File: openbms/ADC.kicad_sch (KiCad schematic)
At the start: 117 parts, among them U1 DMP68D1LVQ-7, U10 DMP68D1LVQ-7, U11 DMN601VK-7, U12 DMN601VK-7, U13 DMN601VK-7, U14 DMN601VK-7, U2 DMP68D1LVQ-7, U3 DMN601VK-7, U4 DMP68D1LVQ-7, U5 ADS131M08xPBS, U6 DMP68D1LVQ-7, U7 DMN601VK-7, U8 DMP68D1LVQ-7, U9 DMP68D1LVQ-7, Y1 8.192MHz

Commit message: Footprints for pmos/nmos and pmos/pmos packages fixed, charger detection added, pwr_gd and flt_gd lines removed
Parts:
- U5: footprint custom_library:TQFP-32_5x5mm_P0.5mm -> Package_QFP:TQFP-32_5x5mm_P0.5mm
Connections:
- net CELL_6_M: now also U14.6; no longer U14.3
- net CELL_7_M: now also U14.3; no longer U14.6
- net GND: no longer R15.1, R16.1, R36.1, R37.1, R60.1, R61.1, R73.1, R77.1
- net GND_BATT_CELL: now also R15.1, R16.1, R36.1, R37.1, R60.1, R61.1, R73.1, R77.1
- net at R66.2, U10.5: now also U11.6; no longer U11.3
- net at U1.3: now also R11.2; no longer R10.2
- net at U1.6: now also R10.2; no longer R11.2
- net at R69.2: now also U10.3; no longer U10.6
- net at R28.2: now also U4.3; no longer U4.6
- net at D1.3 (K), D2.3 (K), D3.3 (K): now also U11.3; no longer U11.6
- net at U2.3: now also R13.2; no longer R12.2
- net at U2.6: now also R12.2; no longer R13.2
- net at U6.3: now also R42.2; no longer R41.2
- net at U6.6: now also R41.2; no longer R42.2
- net at R67.2: now also U9.6; no longer U9.3
- net at U8.3: now also R57.2; no longer R56.2
- net at U8.6: now also R56.2; no longer R57.2
- net at U3.3: now also R7.1; no longer R6.1
- net at U3.6: now also R6.1; no longer R7.1
- net at R68.2: now also U9.3; no longer U9.6
- net at R64.1: now also U12.6; no longer U12.3
- net at R34.1: now also U7.6; no longer U7.3
- net at R27.2: now also U4.6; no longer U4.3
- net at R74.1: now also U13.6; no longer U13.3
- net at R35.1: now also U7.3; no longer U7.6
- net at R65.1: now also U12.3; no longer U12.6

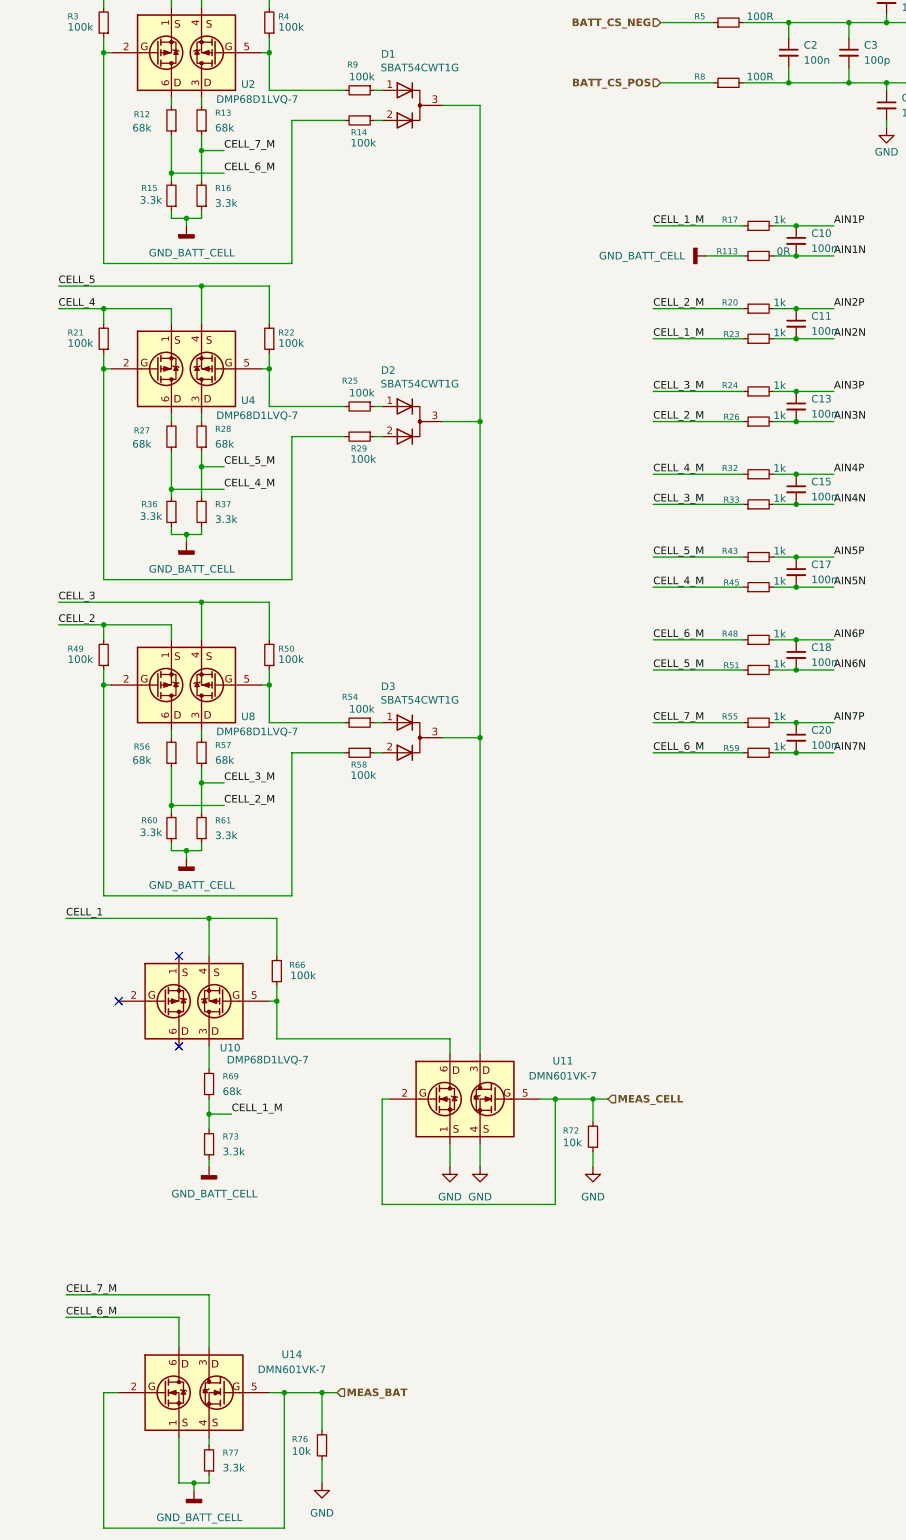
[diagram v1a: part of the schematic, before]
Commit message: Resistor dividers updated and put to 0.1% tolerance
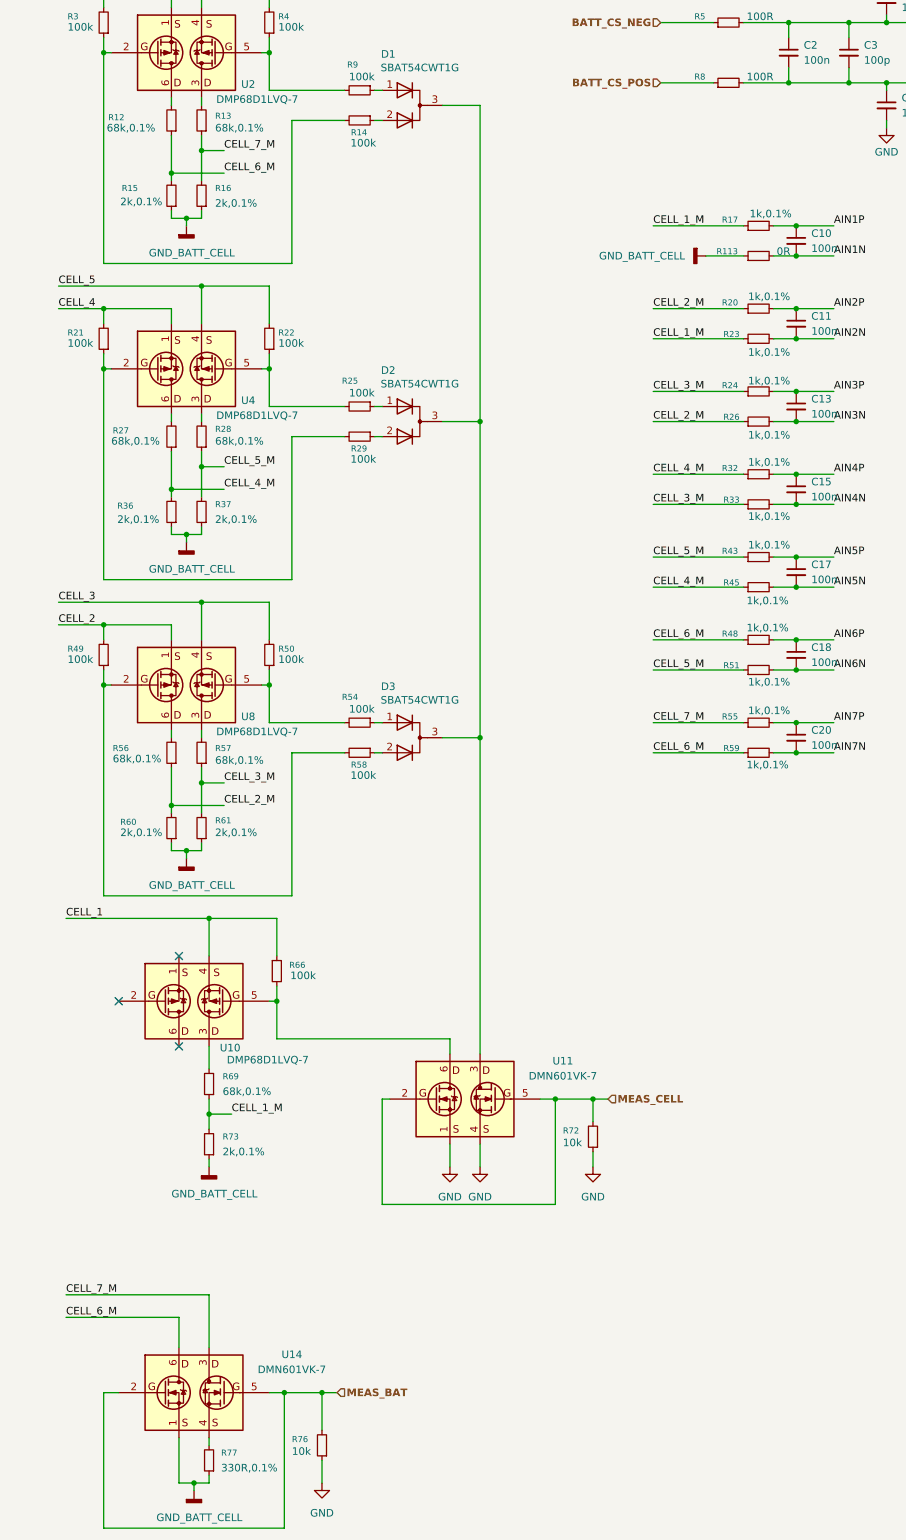
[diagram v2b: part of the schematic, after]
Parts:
- R12, R13, R27, R28, R56, R57, R69: value 68k -> 68k,0.1%; Manufacturer_Part_Number RMCF0402FT68K0 -> RT0402BRD0768KL
- R15, R16, R36, R37, R60, R61, R73: value 3.3k -> 2k,0.1%; Manufacturer_Part_Number ERA-2AEB332X -> RT0402BRD072KL
- R17, R20, R23, R24, R26, R32, R33, R43, R45, R48, R51, R55, R59: value 1k -> 1k,0.1%; Manufacturer_Part_Number RMCF0402FT1K00 -> RT0402BRD071KL
- R77: value 3.3k -> 330R,0.1%; Manufacturer_Part_Number ERA-2AEB332X -> RT0402BRD07330RL

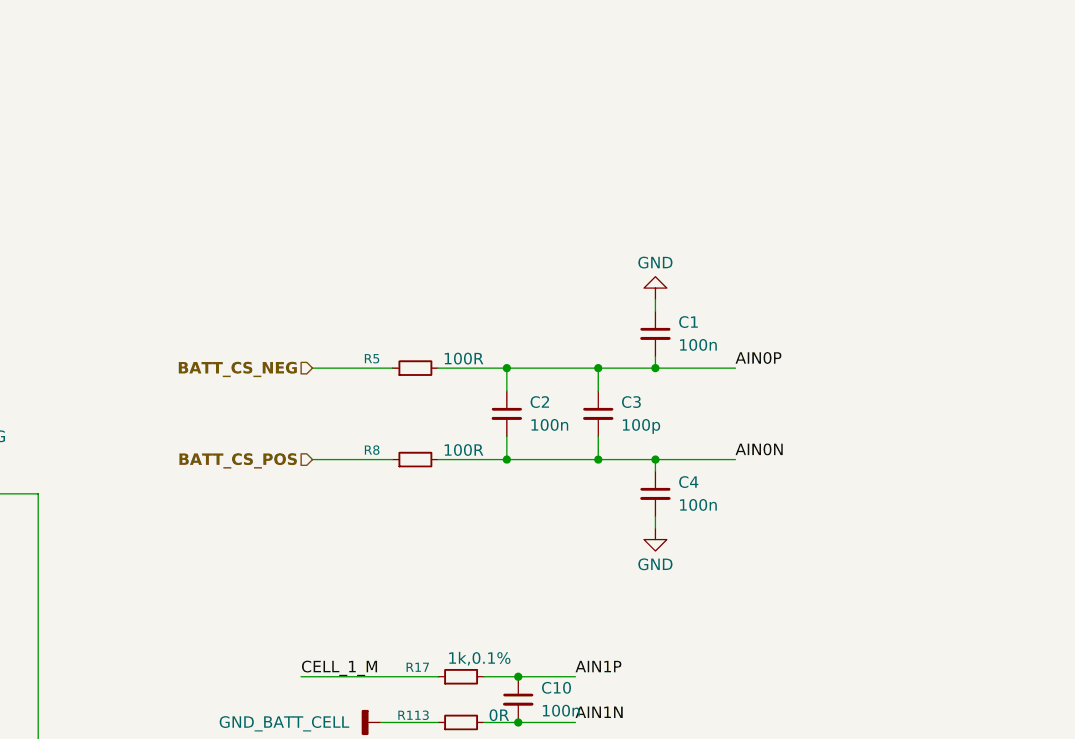
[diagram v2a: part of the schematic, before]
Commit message: Option to shortcut current ADC sensor added
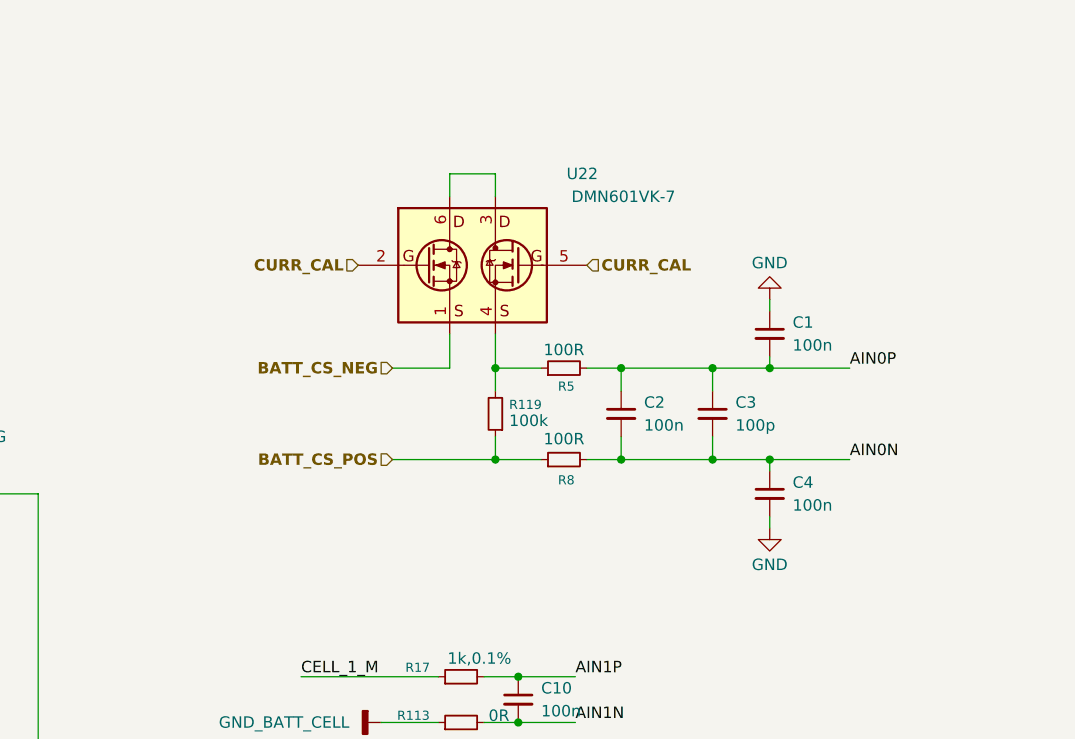
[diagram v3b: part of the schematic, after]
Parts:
- added R119: 100k, Resistor_SMD:R_0402_1005Metric, symbol Device:R_Small
- added U22: DMN601VK-7, custom_library:SOTFL50P162X60-6N, symbol custom_library:DMN601VK-7
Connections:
- net BATT_CS_NEG: now also U22.1; no longer R5.1
- net BATT_CS_POS: now also R119.1
- new net: R119.2, R5.1, U22.4
- new net: U22.3, U22.6
- new net CURR_CAL: U22.2, U22.5
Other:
- moved on the sheet: C1, C2, C3, C4, R5, R8

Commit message: Button for quick enable added
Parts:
- U5: footprint Package_QFP:TQFP-32_5x5mm_P0.5mm -> custom_library:TQFP-32_5x5mm_P0.5mm
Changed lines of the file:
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@@
 			)
 		)
-		(property "Footprint" "Package_QFP:TQFP-32_5x5mm_P0.5mm"
+		(property "Footprint" "custom_library:TQFP-32_5x5mm_P0.5mm"
 			(at 494.03 255.27 0)
 			(effects

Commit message: Green LED part number fixed,  PCB mask color updated, project description updated
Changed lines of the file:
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@@
 	(title_block
 		(title "OpenBMS")
-		(date "2026-03-24")
-		(rev "A")
+		(date "2026-09-24")
+		(rev "B")
 		(comment 2 "More at openbatt.dev")
 		(comment 3 "Designed by OpenBatt team")
@@
 		)
 	)
-	(text_box "About:\n- ADC circuit for battery voltage and current reading\n- Cell FETs for cell balancing\n\nDesign Parameters:\n- 7-cell battery voltage monitoring (between 2.5V and 4.3V)\n- 7-cell battery balancing (up to 86mA per cell)\n- Current monitoring (up to 20A)\n\nHow to use it:\n1) Battery cells are disabled from ADC by default to disable current leaking from battery when BMS is off. To enable battery reading, set MEAS_CELL to 1\n2) Read differential AINxP - AINxN voltage and multiply with 71.3/3.3 = 21.606 to get batter cell voltage in V\n3) Read battery current by reading voltage between AIN0P and AIN0N. Divide voltage by 0.001 (shunt resisot is 1m ohm) to get current in A\n4) There is a special case to read overall battery voltage by setting MEAS_BATT to 1 (while keeping MEAS_CELL at 1) and read voltage between AIN7P and AIN7N (like you would read cell 7) and multiply result with 74.6/6.6 = 11.303\n5) Balancing circuit for each sell can be enabled individually by setting CELL_x_BAL to 1. While balancer (cell FET) is on, don't read battery voltage, as you could get less precise cell voltage\n"
+	(text_box "About:\n- ADC circuit for battery voltage and current reading\n- Cell FETs for cell balancing\n\nDesign Parameters:\n- 7-cell battery voltage monitoring (between 2.5V and 4.3V)\n- 7-cell battery balancing (up to 86mA per cell)\n- Current monitoring (up to 20A)\n\nHow to use it:\n1) Battery cells are disabled from ADC by default to disable current leaking from battery when BMS is off. To enable battery reading, set MEAS_CELL to 1\n2) Read differential AINxP - AINxN voltage and multiply with (68+2)/2 = 35 to get batter cell voltage in V\n3) Read battery current by reading voltage between AIN0P and AIN0N. Divide voltage by 0.002 (shunt resisot is 2m ohm) to get current in A\n4) There is a special case to read overall battery voltage by setting MEAS_BATT to 1 (while keeping MEAS_CELL at 1) and read voltage between AIN7P and AIN7N (like you would read cell 7)\n5) Balancing circuit for each sell can be enabled individually by setting CELL_x_BAL to 1. While balancer (cell FET) is on, don't read battery voltage, as you could get less precise cell voltage\n"
 		(exclude_from_sim no)
 		(at 20.32 20.32 0)
